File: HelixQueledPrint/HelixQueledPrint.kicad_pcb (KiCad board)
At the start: 4 copper layers, 47.1 x 43.3 mm, 133 parts, among them J1 USB_C_Receptacle_USB2.0_16P, J101 Conn_Coaxial, J601 Screw_Terminal_01x02, SW1 SW_SPST, SW2 SW_SPST, U1 CH224D, U101 ESP32-C6FHx, U202 TPS92201, U302 TPS92201, U402 TPS92201, U502 TPS92201, U601 MB34F, U602 SY8366H, U603 XBL1117, Y1 40MHz

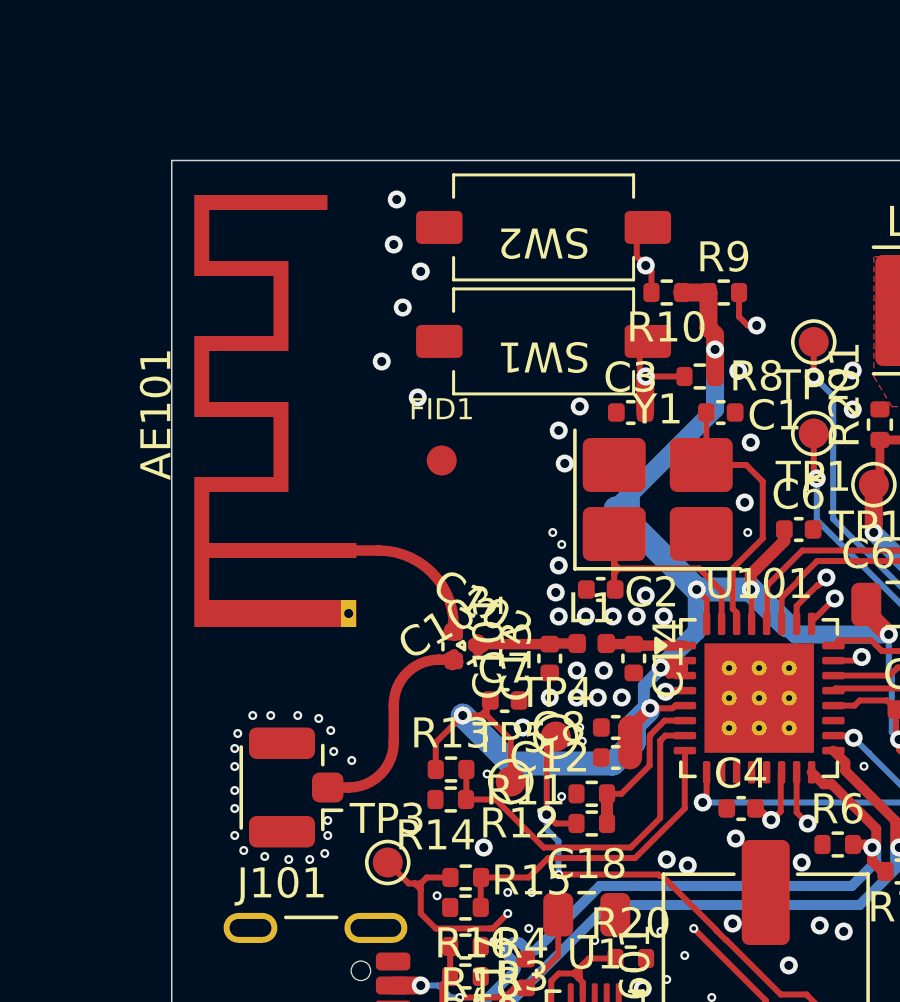
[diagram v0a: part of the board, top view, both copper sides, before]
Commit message: fixed rf path
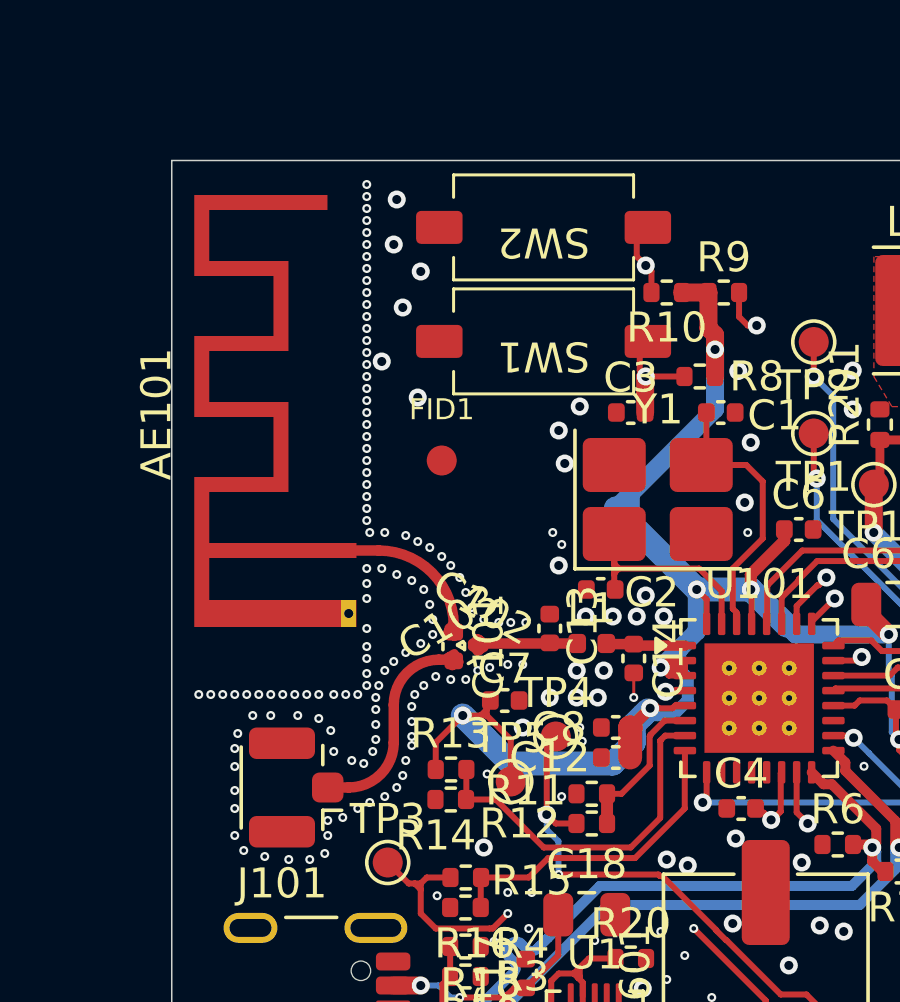
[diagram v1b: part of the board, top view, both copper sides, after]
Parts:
- moved C13 1.00 mm to (117.7, 54.1), turned to 90 degrees
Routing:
- net +3V3: track 103.9 -> 106.8 mm
- net GND: track 4.20 -> 5.02 mm, vias 239 -> 340

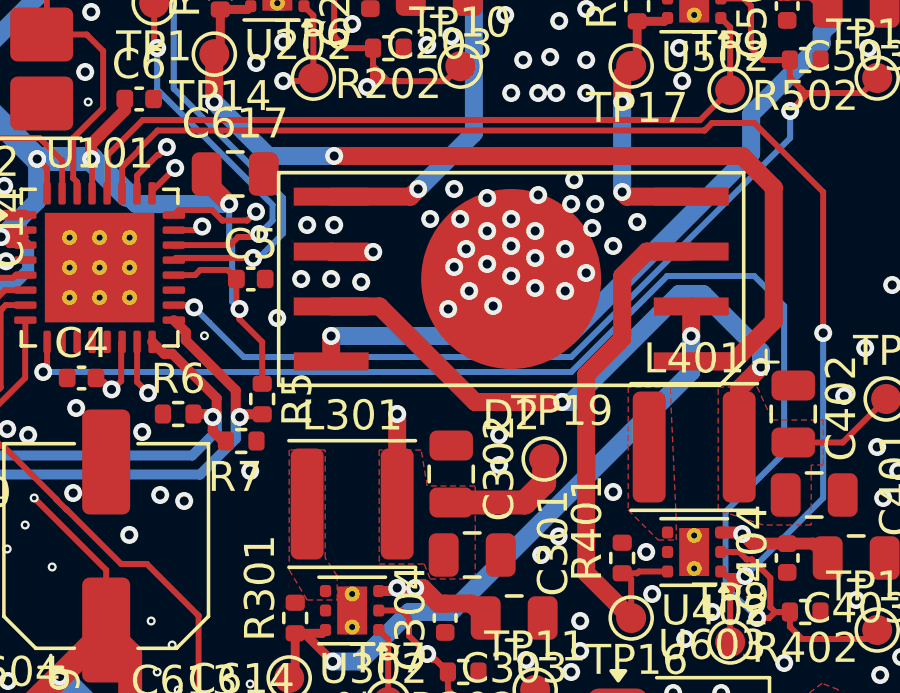
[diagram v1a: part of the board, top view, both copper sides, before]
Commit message: fixed led polarity
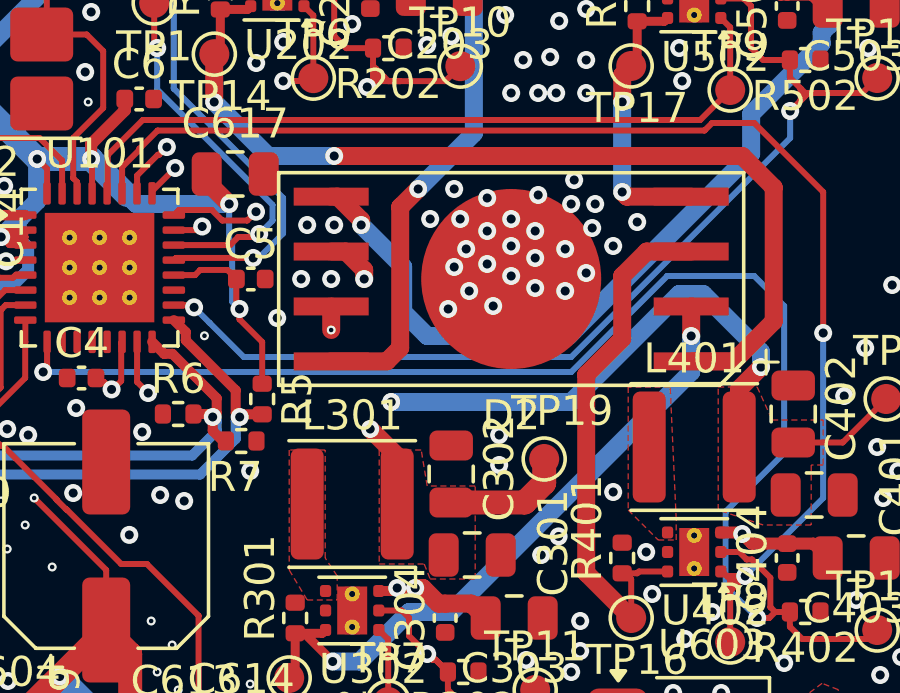
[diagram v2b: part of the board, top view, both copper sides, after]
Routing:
- net /LedDriverRed/LED+: track 19.1 -> 24.2 mm
- net /LedDriverGreen/LED+: track 14.6 -> 11.7 mm
- net /LedDriverBlue/LED+: track 25.1 -> 27.9 mm, vias 2 -> 3
- net /LedDriverWhite/LED+: track 31.4 -> 33.4 mm
- net GND: vias 340 -> 339
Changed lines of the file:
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@@
 		)
 		(pad "5" smd rect
-			(at 2.745 -6 90)
+			(at -2.745 -6 90)
 			(size 0.6 2.5)
 			(layers "F.Cu" "F.Mask" "F.Paste")
@@
 		)
 		(pad "6" smd rect
-			(at 0.915 -6 90)
+			(at -0.915 -6 90)
 			(size 0.6 2.5)
 			(layers "F.Cu" "F.Mask" "F.Paste")
@@
 		)
 		(pad "7" smd rect
-			(at -0.915 -6 90)
+			(at 0.915 -6 90)
 			(size 0.6 2.5)
 			(layers "F.Cu" "F.Mask" "F.Paste")
@@
 		)
 		(pad "8" smd rect
-			(at -2.745 -6 90)
+			(at 2.745 -6 90)
 			(size 0.6 2.5)
 			(layers "F.Cu" "F.Mask" "F.Paste")
@@
 	)
 	(via
-		(at 133.4 56.9)
-		(size 0.6)
-		(drill 0.3)
-		(layers "F.Cu" "B.Cu")
-		(remove_unused_layers yes)
-		(keep_end_layers yes)
-		(free yes)
-		(zone_layer_connections "In1.Cu" "In2.Cu")
-		(net 2)
-	)
-	(via
 		(at 111.6 49.3)
 		(size 0.3)
@@
 	)
 	(segment
-		(start 132.4 54.055)
-		(end 135.045 54.055)
+		(start 134.7 54.4)
+		(end 134.7 59.1)
 		(width 0.6)
 		(layer "F.Cu")
@@
 	)
 	(segment
-		(start 135.045 54.055)
-		(end 135.3 53.8)
+		(start 134.255 59.545)
+		(end 132.4 59.545)
+		(width 0.6)
+		(layer "F.Cu")
+		(net 9)
+	)
+	(segment
+		(start 135.3 53.8)
+		(end 134.7 54.4)
+		(width 0.6)
+		(layer "F.Cu")
+		(net 9)
+	)
+	(segment
+		(start 134.7 59.1)
+		(end 134.255 59.545)
 		(width 0.6)
 		(layer "F.Cu")
@@
 	)
 	(segment
-		(start 134.6 64.3)
-		(end 134.6 61.3)
+		(start 132.4 57.715)
+		(end 132.4 58.5)
 		(width 0.6)
 		(layer "F.Cu")
@@
 	)
 	(segment
-		(start 139.5 63.6)
-		(end 139.5 62.8)
-		(width 0.8)
+		(start 133.7 61.8)
+		(end 134.6 62.7)
+		(width 0.6)
 		(layer "F.Cu")
 		(net 11)
 	)
 	(segment
-		(start 132.415 55.9)
-		(end 132.4 55.885)
-		(width 0.6)
+		(start 139.5 63.6)
+		(end 139.5 62.8)
+		(width 0.8)
 		(layer "F.Cu")
 		(net 11)
 	)
 	(segment
-		(start 133.8 55.9)
-		(end 132.415 55.9)
+		(start 134.6 62.7)
+		(end 134.6 64.3)
 		(width 0.6)
 		(layer "F.Cu")
@@
 	)
 	(via
-		(at 133.8 55.9)
+		(at 133.7 61.8)
 		(size 0.6)
 		(drill 0.3)
 		(layers "F.Cu" "B.Cu")
-		(remove_unused_layers yes)
-		(keep_end_layers yes)
-		(zone_layer_connections)
 		(net 11)
 	)
 	(via
-		(at 134.6 61.3)
-		(size 0.6)
-		(drill 0.3)
+		(at 132.4 58.5)
+		(size 0.3)
+		(drill 0.15)
 		(layers "F.Cu" "B.Cu")
-		(remove_unused_layers yes)
-		(keep_end_layers yes)
-		(zone_layer_connections)
 		(net 11)
 	)
 	(segment
-		(start 134.6 56.2)
-		(end 134.6 61.3)
+		(start 132.4 58.5)
+		(end 132.4 60.5)
 		(width 0.6)
 		(layer "In2.Cu")
@@
 	)
 	(segment
-		(start 134.3 55.9)
-		(end 134.6 56.2)
-		(width 0.6)
-		(layer "In2.Cu")
-		(net 11)
-	)
-	(segment
-		(start 133.8 55.9)
-		(end 134.3 55.9)
+		(start 132.4 60.5)
+		(end 133.7 61.8)
 		(width 0.6)
 		(layer "In2.Cu")
@@
 	)
 	(segment
-		(start 132.4 57.715)
-		(end 134.015 57.715)
+		(start 133.5 56.5)
+		(end 132.9 55.9)
 		(width 0.6)
 		(layer "F.Cu")
@@
 	)
 	(segment
-		(start 147.8 62.25)
-		(end 149.45 62.25)
-		(width 0.2)
+		(start 133.5 56.8)
+		(end 133.5 56.5)
+		(width 0.6)
 		(layer "F.Cu")
 		(net 12)
 	)
 	(segment
-		(start 137.2 60.9)
-		(end 140.1 60.9)
-		(width 0.6)
+		(start 147.8 62.25)
+		(end 149.45 62.25)
+		(width 0.2)
 		(layer "F.Cu")
 		(net 12)
@@
 	)
 	(segment
-		(start 134.015 57.715)
-		(end 137.2 60.9)
+		(start 132.4 55.885)
+		(end 132.885 55.885)
+		(width 0.6)
+		(layer "F.Cu")
+		(net 12)
+	)
+	(segment
+		(start 132.885 55.885)
+		(end 132.9 55.9)
 		(width 0.6)
 		(layer "F.Cu")
@@
 	)
 	(via
-		(at 140.1 60.9)
+		(at 134.4 60.9)
+		(size 0.6)
+		(drill 0.3)
+		(layers "F.Cu" "B.Cu")
+		(net 12)
+	)
+	(via
+		(at 133.5 56.8)
 		(size 0.6)
 		(drill 0.3)
 		(layers "F.Cu" "B.Cu")
-		(remove_unused_layers yes)
-		(keep_end_layers yes)
-		(zone_layer_connections)
 		(net 12)
 	)
@@
 	)
 	(segment
+		(start 140.1 60.9)
+		(end 134.4 60.9)
+		(width 0.6)
+		(layer "B.Cu")
+		(net 12)
+	)
+	(segment
 		(start 144 57.3)
 		(end 144.8 57.3)
@@
 	)
 	(segment
+		(start 134.4 57.7)
+		(end 133.5 56.8)
+		(width 0.6)
+		(layer "In2.Cu")
+		(net 12)
+	)
+	(segment
+		(start 134.4 60.9)
+		(end 134.4 57.7)
+		(width 0.6)
+		(layer "In2.Cu")
+		(net 12)
+	)
+	(segment
 		(start 150.25 43.85)
 		(end 150.9 43.2)
@@
 	)
 	(segment
-		(start 132.4 59.545)
-		(end 132.4 58.7)
+		(start 133.4 55)
+		(end 133.4 54.837925)
+		(width 0.6)
+		(layer "F.Cu")
+		(net 13)
+	)
+	(segment
+		(start 132.617075 54.055)
+		(end 132.4 54.055)
 		(width 0.6)
 		(layer "F.Cu")
@@
 		(net 13)
 	)
+	(segment
+		(start 133.4 54.837925)
+		(end 132.617075 54.055)
+		(width 0.6)
+		(layer "F.Cu")
+		(net 13)
+	)
 	(via
 		(at 149 43.85)
@@
 	)
 	(via
-		(at 132.4 58.7)
+		(at 133.4 55)
 		(size 0.6)
 		(drill 0.3)
 		(layers "F.Cu" "B.Cu")
-		(remove_unused_layers yes)
-		(keep_end_layers yes)
-		(zone_layer_connections)
+		(net 13)
+	)
+	(segment
+		(start 148.749 48.951)
+		(end 148.749 48.588925)
+		(width 0.6)
+		(layer "B.Cu")
+		(net 13)
+	)
+	(segment
+		(start 140.320768 58.7)
+		(end 146.4 52.620768)
+		(width 0.6)
+		(layer "B.Cu")
 		(net 13)
 	)
@@
 	)
 	(segment
-		(start 148.749 48.588925)
-		(end 149 48.337925)
+		(start 146.4 51.3)
+		(end 148.749 48.951)
 		(width 0.6)
 		(layer "B.Cu")
@@
 	)
 	(segment
-		(start 148.749 48.951)
-		(end 148.749 48.588925)
+		(start 146.4 52.620768)
+		(end 146.4 51.3)
 		(width 0.6)
 		(layer "B.Cu")
@@
 	)
 	(segment
-		(start 132.4 58.7)
-		(end 140.320768 58.7)
+		(start 134.8 56.4)
+		(end 134.8 57.9)
 		(width 0.6)
 		(layer "B.Cu")
@@
 	)
 	(segment
-		(start 146.4 51.3)
-		(end 148.749 48.951)
+		(start 134.8 57.9)
+		(end 135.6 58.7)
 		(width 0.6)
 		(layer "B.Cu")
@@
 	)
 	(segment
-		(start 146.4 52.620768)
-		(end 146.4 51.3)
+		(start 133.4 55)
+		(end 134.8 56.4)
 		(width 0.6)
 		(layer "B.Cu")
@@
 	)
 	(segment
-		(start 140.320768 58.7)
-		(end 146.4 52.620768)
+		(start 148.749 48.588925)
+		(end 149 48.337925)
+		(width 0.6)
+		(layer "B.Cu")
+		(net 13)
+	)
+	(segment
+		(start 135.6 58.7)
+		(end 140.320768 58.7)
 		(width 0.6)
 		(layer "B.Cu")
@@
 			"6d1905e3-3fa0-48b3-8ed8-63a36d80fa47" "7217303d-d990-449b-93a1-da9b24d5ee79"
 			"77c4820d-a833-4a8f-8dcf-d8db18f78af0" "7bf05bab-0d1a-42c1-8212-240f3a5c3224"
-			"7d403541-f5e3-42f6-bda6-34caff7236bd" "7f5dbca1-b497-4283-82f1-cba4d5b8d9b8"
-			"8467b335-d516-498d-81ee-4a5f2a47267d" "880050ae-1411-49f9-bf3d-af733427d158"
-			"8859e957-dac8-4fef-9295-1bbddc9e28a1" "924b7717-60d7-4e14-bcbf-16569a720f6d"
-			"980fdde5-c7b6-4337-87d5-929ae9d6ec17" "9953d017-1b30-4071-a219-f49106d4c71f"
-			"9a069d9b-391c-4b0a-bb41-faded85f970b" "9a430dfb-1a20-45c9-8d9d-25f5b2d76f13"
-			"9d7fc95e-dc34-49fb-842b-9518f2252af4" "a4abb9e5-9e04-4b85-81ae-6c5d4fc5f14e"
-			"a5cfdac8-b53e-4e9b-bbbd-7b294582cd9f" "a8452db4-9f98-4f08-8ef8-0e3fa7c861ef"
-			"aadf5a1d-bd6c-495a-8fe3-6189d11e8589" "acad617b-743a-4076-abb0-9c3fe7bc55e7"
-			"b80a9a47-b8f5-4933-8d8d-0a438f6a498b" "c3532b1d-c2f7-4ac5-9b7b-e912b20888c8"
-			"c447e533-e64b-4b84-8290-6aaf6bf7b22b" "d5b913eb-4a69-4eea-ac45-2c4da56c2cac"
-			"e04aaa6c-20a9-4421-bce5-6ddac771543b" "e121be6c-bb5a-4183-9d5c-6266474e1fc9"
-			"e4830c6b-ec75-41f6-a704-7c96e9d0c164" "e9b7a6b5-700c-403e-abda-f394caea5d3f"
-			"f378ebfb-4cd5-4f16-911e-79ce25935a92" "f3c41830-6514-4a06-ac7a-347182dcefb5"
-			"f6aae5aa-b21e-4228-930a-b0896d84e488" "f846e07d-86a2-406b-8957-fe202df6afb7"
-			"ff85ea4d-29da-46da-a2ef-b83c40ddb8be"
+			"7f5dbca1-b497-4283-82f1-cba4d5b8d9b8" "8467b335-d516-498d-81ee-4a5f2a47267d"
+			"880050ae-1411-49f9-bf3d-af733427d158" "8859e957-dac8-4fef-9295-1bbddc9e28a1"
+			"924b7717-60d7-4e14-bcbf-16569a720f6d" "980fdde5-c7b6-4337-87d5-929ae9d6ec17"
+			"9953d017-1b30-4071-a219-f49106d4c71f" "9a069d9b-391c-4b0a-bb41-faded85f970b"
+			"9a430dfb-1a20-45c9-8d9d-25f5b2d76f13" "9d7fc95e-dc34-49fb-842b-9518f2252af4"
+			"a4abb9e5-9e04-4b85-81ae-6c5d4fc5f14e" "a5cfdac8-b53e-4e9b-bbbd-7b294582cd9f"
+			"a8452db4-9f98-4f08-8ef8-0e3fa7c861ef" "aadf5a1d-bd6c-495a-8fe3-6189d11e8589"
+			"acad617b-743a-4076-abb0-9c3fe7bc55e7" "b80a9a47-b8f5-4933-8d8d-0a438f6a498b"
+			"c3532b1d-c2f7-4ac5-9b7b-e912b20888c8" "c447e533-e64b-4b84-8290-6aaf6bf7b22b"
+			"d5b913eb-4a69-4eea-ac45-2c4da56c2cac" "e04aaa6c-20a9-4421-bce5-6ddac771543b"
+			"e121be6c-bb5a-4183-9d5c-6266474e1fc9" "e4830c6b-ec75-41f6-a704-7c96e9d0c164"
+			"e9b7a6b5-700c-403e-abda-f394caea5d3f" "f378ebfb-4cd5-4f16-911e-79ce25935a92"
+			"f3c41830-6514-4a06-ac7a-347182dcefb5" "f6aae5aa-b21e-4228-930a-b0896d84e488"
+			"f846e07d-86a2-406b-8957-fe202df6afb7" "ff85ea4d-29da-46da-a2ef-b83c40ddb8be"
 		)
 	)
